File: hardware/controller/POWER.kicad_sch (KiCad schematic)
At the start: 0 parts

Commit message: asdasd
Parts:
- added S1: OS102011MS2QS1, OS102011MS2QS1, symbol SamacSys_Parts:OS102011MS2QS1
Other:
- note added: "todo: 3v3 and 5v"
- note added: "todo: battery level checker"
- note added: "todo: usbc or battery power"
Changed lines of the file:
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@@
 	(generator_version "9.0")
 	(paper "A4")
-	(hierarchical_label "VBUS"
+	(text "todo: battery level checker\n"
+		(exclude_from_sim no)
+		(at 139.954 79.248 0)
+		(effects
+			(font
+				(size 1.27 1.27)
+			)
+		)
+	)
+	(text "todo: usbc or battery power"
+		(exclude_from_sim no)
+		(at 139.192 68.834 0)
+		(effects
+			(font
+				(size 1.27 1.27)
+			)
+		)
+	)
+	(text "todo: 3v3 and 5v\n\n"
+		(exclude_from_sim no)
+		(at 134.62 74.422 0)
+		(effects
+			(font
+				(size 1.27 1.27)
+			)
+		)
+	)
+	(hierarchical_label "USBC_IN"
 		(shape input)
 		(at 170.18 85.09 0)
@@
 		)
 	)
+	(symbol
+		(lib_id "SamacSys_Parts:OS102011MS2QS1")
+		(at 161.29 110.49 0)
+		(unit 1)
+		(exclude_from_sim no)
+		(in_bom yes)
+		(on_board yes)
+		(dnp no)
+		(fields_autoplaced yes)
+		(property "Reference" "S1"
+			(at 180.34 114.2999 0)
+			(effects
+				(font
+					(size 1.27 1.27)
+				)
+				(justify left)
+			)
+		)
+		(property "Value" "OS102011MS2QS1"
+			(at 180.34 116.8399 0)
+			(effects
+				(font
+					(size 1.27 1.27)
+				)
+				(justify left)
+			)
+		)
+		(property "Footprint" "OS102011MS2QS1"
+			(at 180.34 205.41 0)
+			(effects
+				(font
+					(size 1.27 1.27)
+				)
+				(justify left top)
+				(hide yes)
+			)
+		)
+		(property "Datasheet" "https://www.ckswitches.com/media/1428/os.pdf"
+			(at 180.34 305.41 0)
+			(effects
+				(font
+					(size 1.27 1.27)
+				)
+				(justify left top)
+				(hide yes)
+			)
+		)
+		(property "Description" "SWITCH SLIDE SPDT 100MA 12V"
+			(at 161.29 110.49 0)
+			(effects
+				(font
+					(size 1.27 1.27)
+				)
+				(hide yes)
+			)
+		)
+		(property "Height" "8"
+			(at 180.34 505.41 0)
+			(effects
+				(font
+					(size 1.27 1.27)
+				)
+				(justify left top)
+				(hide yes)
+			)
+		)
+		(property "Mouser Part Number" "611-OS102011MS2QS1"
+			(at 180.34 605.41 0)
+			(effects
+				(font
+					(size 1.27 1.27)
+				)
+				(justify left top)
+				(hide yes)
+			)
+		)
+		(property "Mouser Price/Stock" "https://www.mouser.co.uk/ProductDetail/CK/OS102011MS2QS1?qs=WtljUlYws5TrGs9OfHrZYw%3D%3D"
+			(at 180.34 705.41 0)
+			(effects
+				(font
+					(size 1.27 1.27)
+				)
+				(justify left top)
+				(hide yes)
+			)
+		)
+		(property "Manufacturer_Name" "C & K COMPONENTS"
+			(at 180.34 805.41 0)
+			(effects
+				(font
+					(size 1.27 1.27)
+				)
+				(justify left top)
+				(hide yes)
+			)
+		)
+		(property "Manufacturer_Part_Number" "OS102011MS2QS1"
+			(at 180.34 905.41 0)
+			(effects
+				(font
+					(size 1.27 1.27)
+				)
+				(justify left top)
+				(hide yes)
+			)
+		)
+		(pin "3"
+		)
+		(pin "4"
+		)
+		(pin "5"
+		)
+		(pin "2"
+		)
+		(pin "1"
+		)
+		(instances
+			(project ""
+				(path "/869bea87-c885-4ead-826b-3f34ceacafad/e70789ad-230b-4d46-b635-87f45083e468"
+					(reference "S1")
+					(unit 1)
+				)
+			)
+		)
+	)

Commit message: a
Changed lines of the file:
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@@
+		)
+	)
+	(hierarchical_label "VBUS"
+		(shape input)
+		(at 170.18 81.28 0)
+		(effects
+			(font
+				(size 1.27 1.27)
+			)
+			(justify left)
 		)
 	)

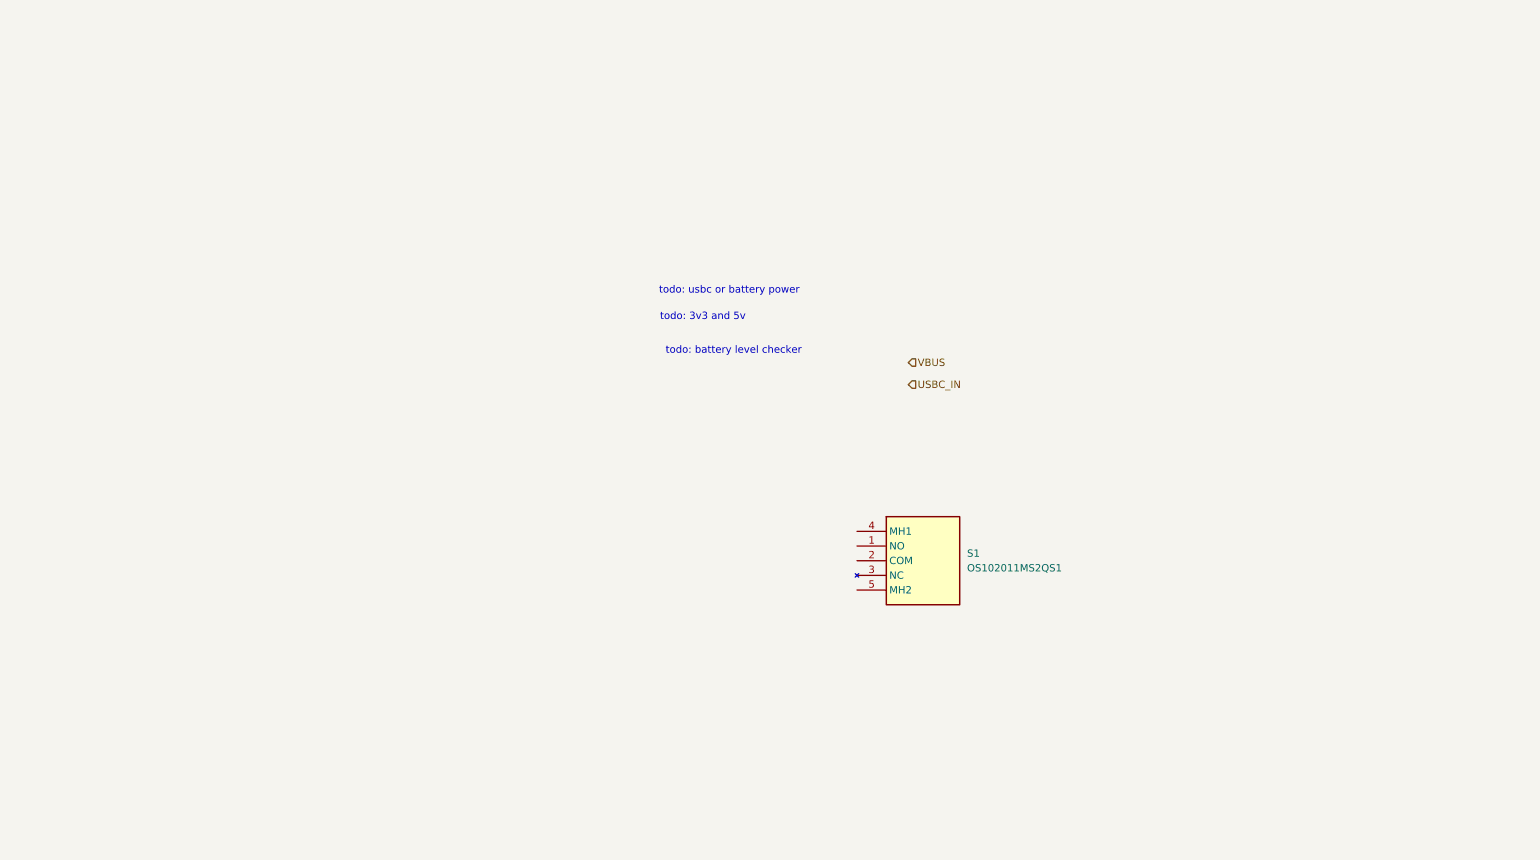
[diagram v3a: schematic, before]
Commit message: modified power circuitry
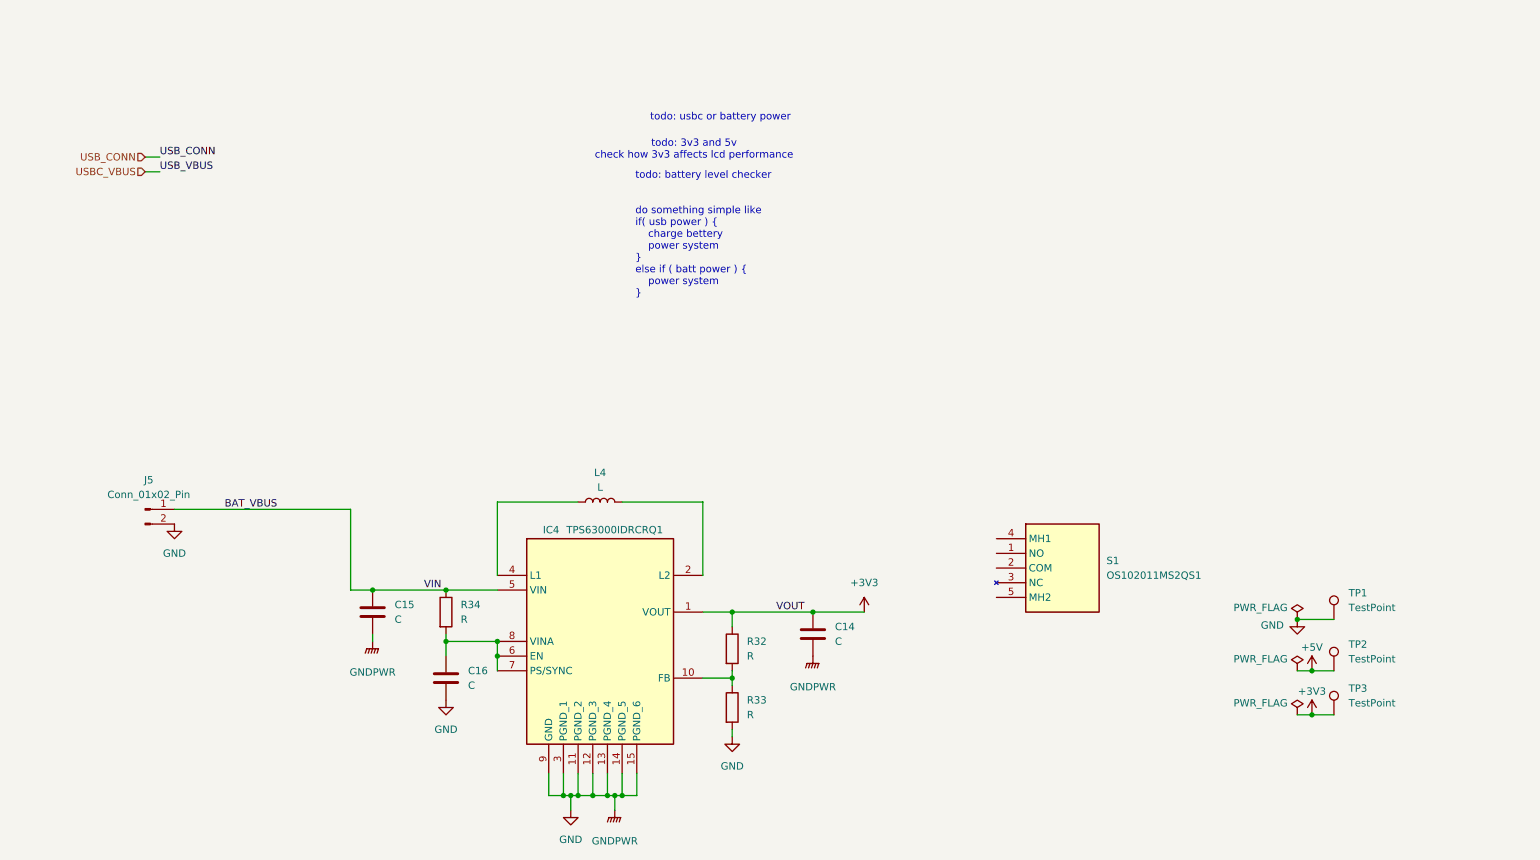
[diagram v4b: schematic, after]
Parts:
- added C14, C15, C16: C, symbol Device:C
- added IC4: TPS63000IDRCRQ1, TPS63000IDRCRQ1, symbol SamacSys_Parts:TPS63000IDRCRQ1
- added J5: Conn_01x02_Pin, symbol Connector:Conn_01x02_Pin
- added L4: L, symbol Device:L
- added R32, R33, R34: R, symbol Device:R
- added TP1, TP2, TP3: TestPoint, symbol Connector:TestPoint
- S1: footprint OS102011MS2QS1 -> SamacSys_Parts:OS102011MS2QS1
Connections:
- new net: IC4.10 (FB), R32.2, R33.1
- new net: C16.1, IC4.6 (EN), IC4.7 (PS/SYNC), IC4.8 (VINA), R34.2
- new net: IC4.4 (L1), L4.1
- new net: IC4.2 (L2), L4.2
- new net +3V3: C14.1, IC4.1 (VOUT), R32.1, TP3.1
- new net +5V: TP2.1
- new net BAT_VBUS: C15.1, IC4.5 (VIN), J5.1 (Pin_1), R34.1
- new net GND: C14.2, C15.2, C16.2, IC4.11 (PGND_2), IC4.12 (PGND_3), IC4.13 (PGND_4), IC4.14 (PGND_5), IC4.15 (PGND_6), IC4.3 (PGND_1), IC4.9 (GND), J5.2 (Pin_2), R33.2, TP1.1
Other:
- note added: "todo: 3v3 and 5v check how 3v3 affects lcd performance"
- note added: "todo: battery level checker do something simple like if( usb power ) { charge bettery power system } else if ( batt power ) { power system }"
- note removed: "todo: 3v3 and 5v"
- note removed: "todo: battery level checker"
- moved on the sheet: S1

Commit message: finished first rev of controller schematic minus actually finding passive components. moved some features to rev2 todo
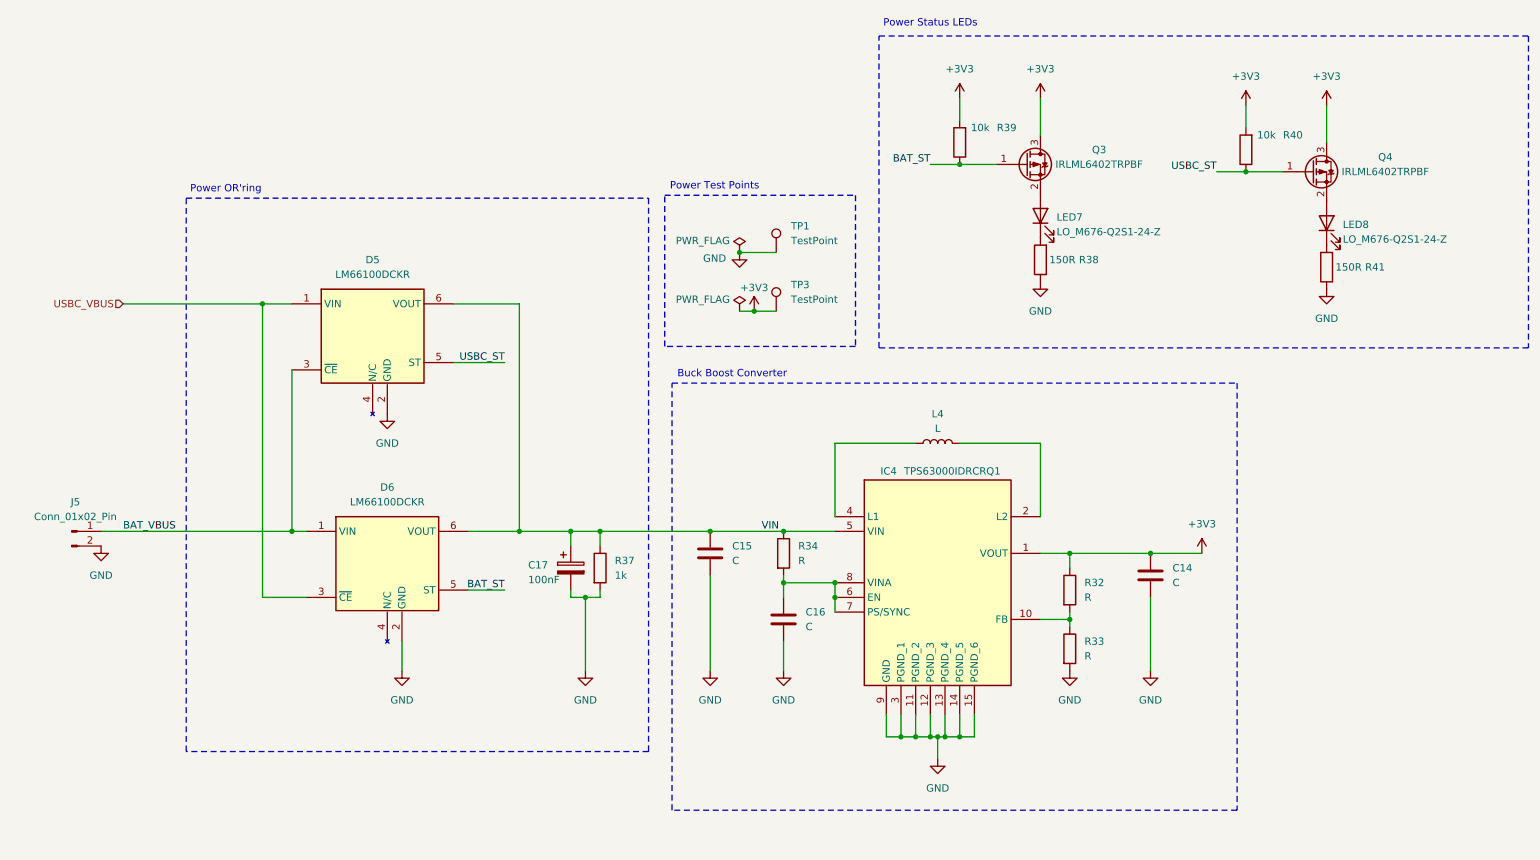
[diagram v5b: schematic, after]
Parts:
- removed S1: OS102011MS2QS1, SamacSys_Parts:OS102011MS2QS1, symbol SamacSys_Parts:OS102011MS2QS1
- removed TP2: TestPoint, symbol Connector:TestPoint
- added C17: 100nF, symbol Device:C_Polarized
- added D5, D6: LM66100DCKR, SamacSys_Parts:SOP65P210X110-6N, symbol SamacSys_Parts:LM66100DCKR
- added LED7, LED8: LO_M676-Q2S1-24-Z, SamacSys_Parts:LEDM2214X140N, symbol Device:LED
- added Q3, Q4: IRLML6402TRPBF, SamacSys_Parts:SOT95P237X112-3N, symbol Transistor_FET:IRLML6402
- added R37: 1k, symbol Device:R
- added R38, R41: 150R, SamacSys_Parts:RESC2012X60N, symbol Device:R
- added R39, R40: 10k, SamacSys_Parts:RESC2012X60N, symbol Device:R
- IC4: footprint TPS63000IDRCRQ1 -> SamacSys_Parts:TPS63000IDRCRQ1
- J5: Mouser Price/Stock (none) -> https://www.mouser.com/ProductDetail/JST-Commercial/B2B-XH-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
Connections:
- net +3V3: now also Q3.3 (D), Q4.3 (D), R39.2, R40.2
- net BAT_VBUS: now also D5.3 (~{CE}), D6.1 (VIN); no longer C15.1, IC4.5 (VIN), R34.1
- net GND: now also C17.2, D5.2 (GND), D6.2 (GND), R37.2, R38.1, R41.1
- net USBC_VBUS: now also D5.1 (VIN), D6.3 (~{CE})
- new net: LED8.2 (A), Q4.2 (S)
- new net: LED8.1 (K), R41.2
- new net: LED7.2 (A), Q3.2 (S)
- new net: LED7.1 (K), R38.2
- new net BAT_ST: D6.5 (ST), Q3.1 (G), R39.1
- new net USBC_ST: D5.5 (ST), Q4.1 (G), R40.1
- new net VIN: C15.1, C17.1, D5.6 (VOUT), D6.6 (VOUT), IC4.5 (VIN), R34.1, R37.1
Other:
- note added: "Buck Boost Converter"
- note added: "Power OR'ring"
- note added: "Power Status LEDs"
- note added: "Power Test Points"
- note removed: "todo: 3v3 and 5v check how 3v3 affects lcd performance"
- note removed: "todo: battery level checker do something simple like if( usb power ) { charge bettery power system } else if ( batt power ) { power system }"
- note removed: "todo: usbc or battery power"
- moved on the sheet: C14, C15, C16, IC4, J5, L4, R32, R33, R34, TP1, TP3

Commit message: Moved LEDs around. Replaced some discrete resistors with resistor arrays. Added mounting holes. Added. Added a lot of actual components for passive elements
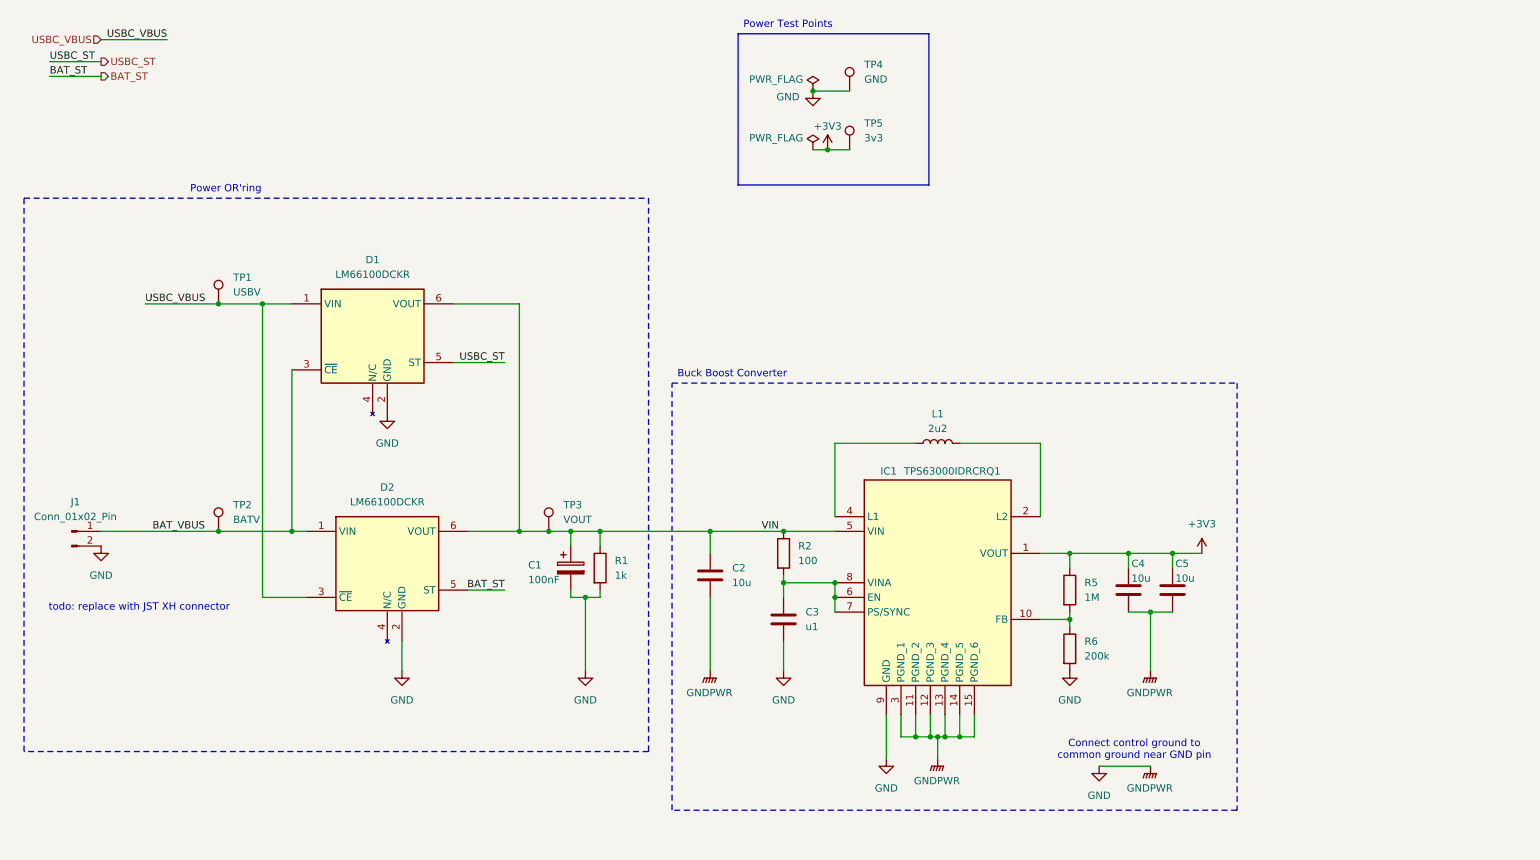
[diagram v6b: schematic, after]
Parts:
- removed L4: L, symbol Device:L
- removed LED7, LED8: LO_M676-Q2S1-24-Z, SamacSys_Parts:LEDM2214X140N, symbol Device:LED
- removed Q3, Q4: IRLML6402TRPBF, SamacSys_Parts:SOT95P237X112-3N, symbol Transistor_FET:IRLML6402
- removed R38, R41: 150R, SamacSys_Parts:RESC2012X60N, symbol Device:R
- removed R39, R40: 10k, SamacSys_Parts:RESC2012X60N, symbol Device:R
- added C5: 10u, CAPC1608X80N, symbol Device:C
- added L1: 2u2, NRS3015T2R2MNGHV, symbol Device:L
- added TP1: USBV, TestPoint:TestPoint_Pad_1.0x1.0mm, symbol Connector:TestPoint
- added TP2: BATV, TestPoint:TestPoint_Pad_1.0x1.0mm, symbol Connector:TestPoint
- added TP3: VOUT, TestPoint:TestPoint_Pad_1.0x1.0mm, symbol Connector:TestPoint
- C2: renamed from C15; value C -> 10u; footprint (none) -> CAPC1608X80N; Height (none) -> 0.8; Manufacturer_Name (none) -> TDK; Manufacturer_Part_Number (none) -> C1608X7T1A106M080AC; Mouser Part Number (none) -> 810-C1608X7T1A106M08; Mouser Price/Stock (none) -> https://www.mouser.co.uk/ProductDetail/TDK/C1608X7T1A106M08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
- C3: renamed from C16; value C -> u1; footprint (none) -> MAJx16; Manufacturer_Name (none) -> TAIYO YUDEN; Manufacturer_Part_Number (none) -> MAJCH168BB7104KTEA01; Mouser Part Number (none) -> 963-MAJCH168BB7104KT; Mouser Price/Stock (none) -> https://www.mouser.co.uk/ProductDetail/TAIYO-YUDEN/MAJCH168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
- C4: renamed from C14; value C -> 10u; footprint (none) -> CAPC1608X80N; Height (none) -> 0.8; Manufacturer_Name (none) -> TDK; Manufacturer_Part_Number (none) -> C1608X7T1A106M080AC; Mouser Part Number (none) -> 810-C1608X7T1A106M08; Mouser Price/Stock (none) -> https://www.mouser.co.uk/ProductDetail/TDK/C1608X7T1A106M08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
- D1: renamed from D5; footprint SamacSys_Parts:SOP65P210X110-6N -> SOP65P210X110-6N
- D2: renamed from D6; footprint SamacSys_Parts:SOP65P210X110-6N -> SOP65P210X110-6N
- IC1: renamed from IC4; footprint SamacSys_Parts:TPS63000IDRCRQ1 -> TPS63000IDRCRQ1
- R1: renamed from R37; footprint (none) -> RESC3116X65N; Height (none) -> 0.65; Manufacturer_Name (none) -> YAGEO; Manufacturer_Part_Number (none) -> RC1206FR-131KL; Mouser Part Number (none) -> 603-RC1206FR-131KL; Mouser Price/Stock (none) -> https://www.mouser.co.uk/ProductDetail/YAGEO/RC1206FR-131KL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
- R2: renamed from R34; value R -> 100
- R5: renamed from R32; value R -> 1M
- R6: renamed from R33; value R -> 200k
- TP4: renamed from TP1; value TestPoint -> GND; footprint (none) -> TestPoint:TestPoint_Pad_1.0x1.0mm
- TP5: renamed from TP3; value TestPoint -> 3v3; footprint (none) -> TestPoint:TestPoint_Pad_1.0x1.0mm
- renumbered C17 to C1, J5 to J1
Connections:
- net +3V3: now also C5.1
- net BAT_VBUS: now also TP2.1
- net GND: now also C5.2
- net USBC_VBUS: now also TP1.1
- net VIN: now also TP3.1
- net at IC1.4 (L1): now also L1.1
- net at IC1.2 (L2): now also L1.2
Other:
- note added: "Connect control ground to common ground near GND pin"
- note added: "todo: replace with JST XH connector"
- note removed: "Power Status LEDs"
- moved on the sheet: C2, C4, TP4, TP5
